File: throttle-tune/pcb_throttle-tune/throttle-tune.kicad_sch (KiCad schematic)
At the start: 49 parts, among them IC1 ATMEGA8A-P, J1 3speedSw-in, J10 9V supply / small battery, J2 gas-pedal-in, J3 throttle-out, J4 3speedSw-out, J5 UART [TX, RX, GND], J7 gpio-reserve, J8 reserve, reverse-sw, J9 5V/GND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

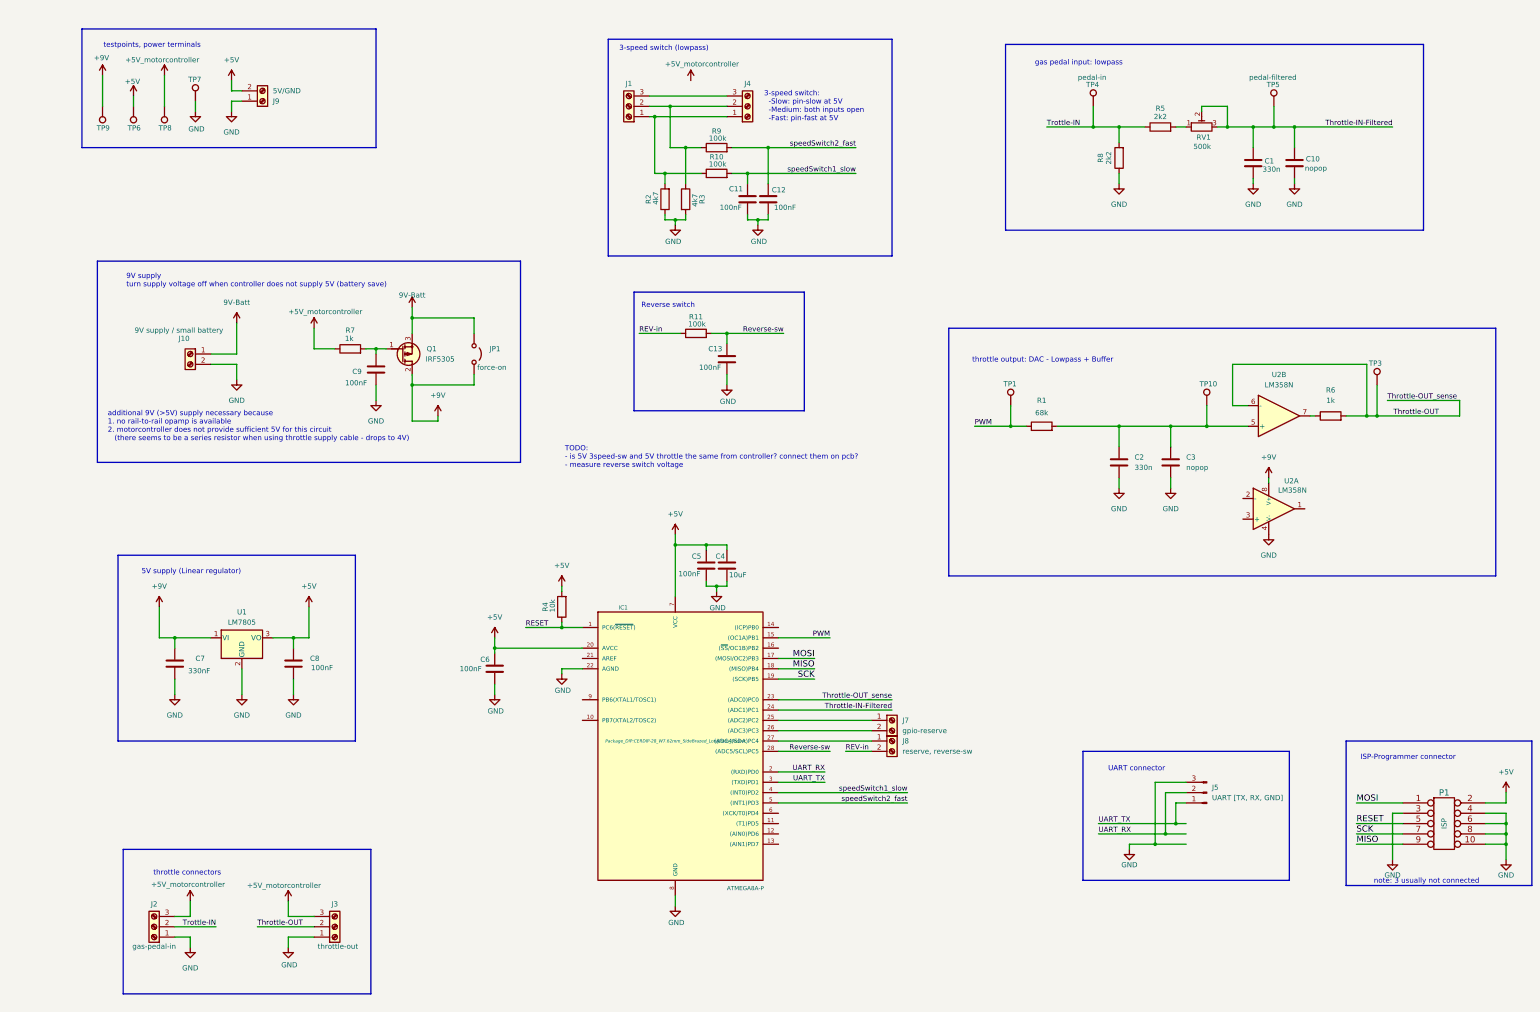
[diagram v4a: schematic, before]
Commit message: pcb: fix supply cutoff (add NPN), update layout
Note: fixed in already milled pcb by adding transistor with wires
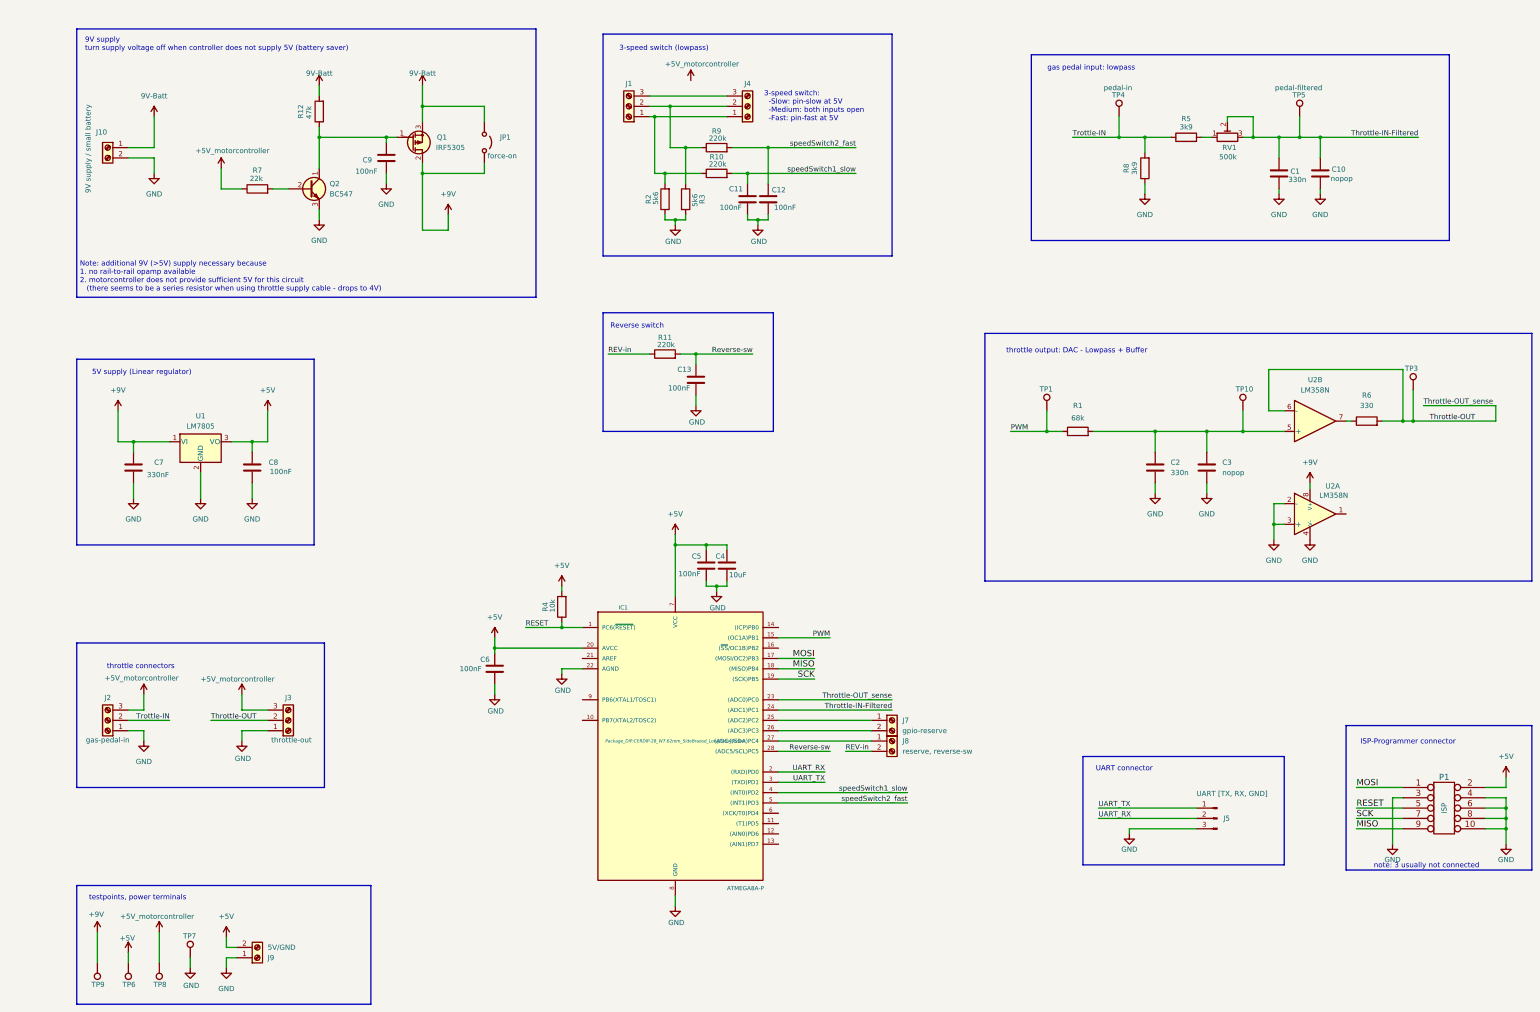
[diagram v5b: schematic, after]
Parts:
- added Q2: BC547, Package_TO_SOT_THT_AKL:TO-92_Inline_Wide_CBE, symbol Transistor_BJT_AKL:BC547
- added R12: 47k, Resistor_THT:R_Axial_DIN0207_L6.3mm_D2.5mm_P10.16mm_Horizontal, symbol Device:R
- R10, R11, R9: value 100k -> 220k
- R2, R3: value 4k7 -> 5k6
- R5, R8: value 2k2 -> 3k9
- R6: value 1k -> 330
- R7: value 1k -> 22k
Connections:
- net 9V-Batt: now also R12.2
- net GND: now also U2.2 (-), U2.3 (+), Q2.3 (E)
- net at C9.1, Q1.1 (G): now also Q2.1 (C), R12.1; no longer R7.2
- new net: Q2.2 (B), R7.2
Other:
- note added: "9V supply turn supply voltage off when controller does not supply 5V (battery saver)"
- note added: "Note: additional 9V (>5V) supply necessary because 1. no rail-to-rail opamp available 2. motorcontroller does not provide sufficient 5V for this circuit (there seems to be a series resistor when using throttle supply cable - drops to 4V)"
- note removed: "9V supply turn supply voltage off when controller does not supply 5V (battery save)"
- note removed: "TODO: - is 5V 3speed-sw and 5V throttle the same from controller? connect them on pcb? - measure reverse switch voltage"
- note removed: "additional 9V (>5V) supply necessary because 1. no rail-to-rail opamp is available 2. motorcontroller does not provide sufficient 5V for this circuit (there seems to be a series resistor when using throttle supply cable - drops to 4V)"
- moved on the sheet: C1, C10, C13, C2, C3, C7, C8, C9, J10, J2, J3, J5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

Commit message: pcb: optimize text, comments, Add README
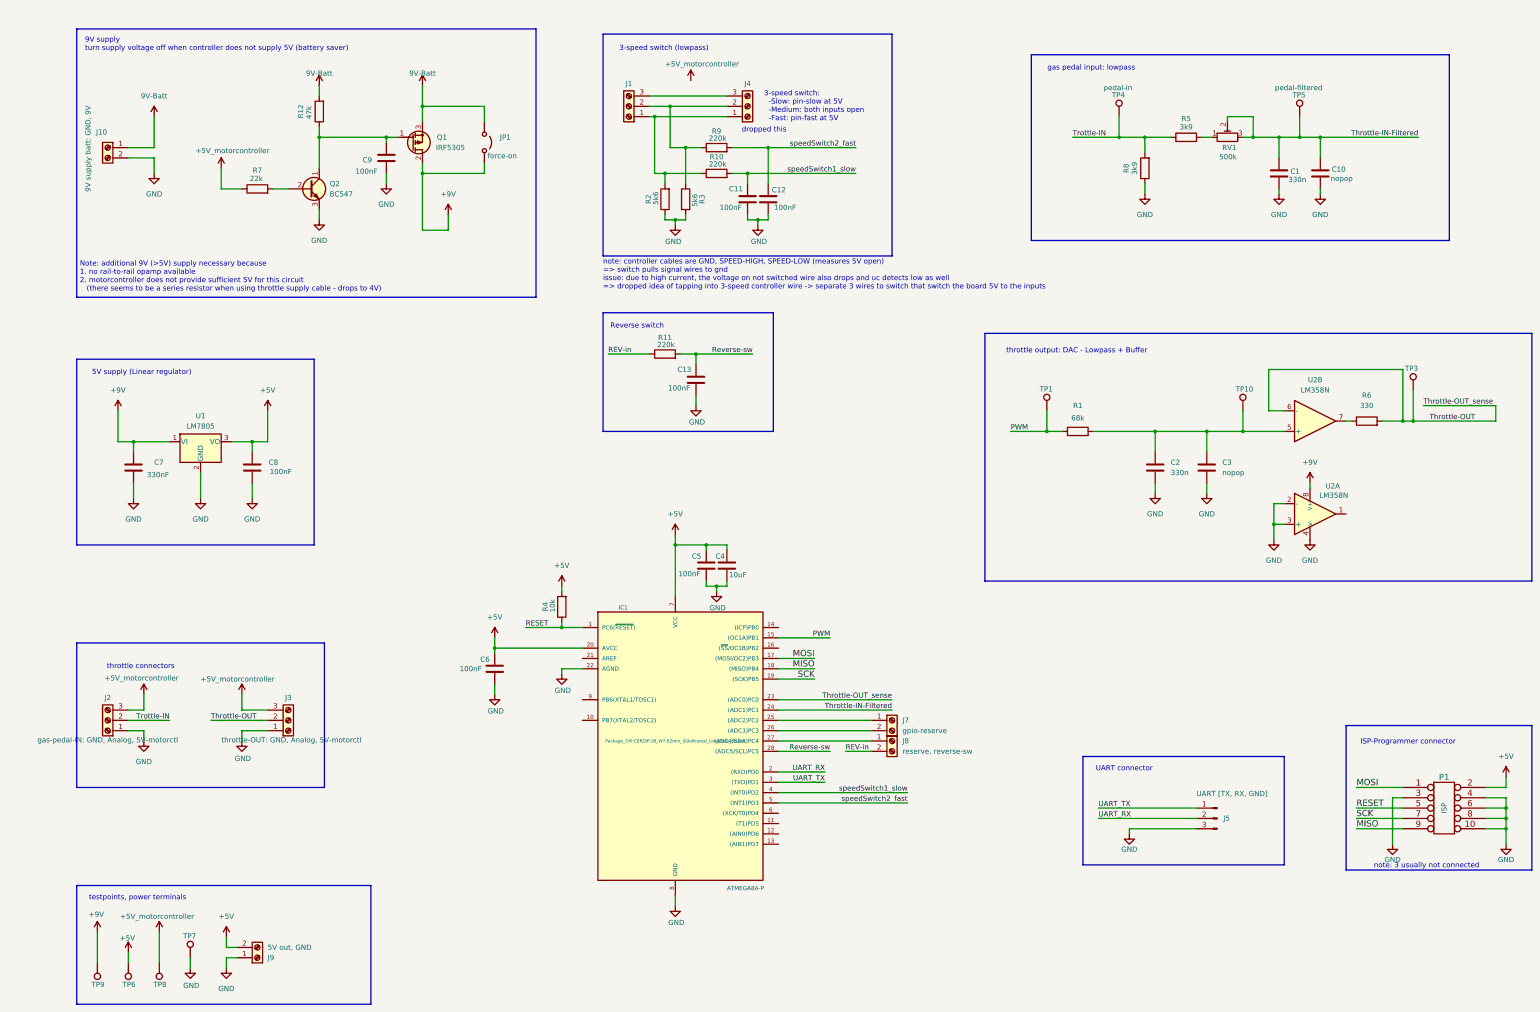
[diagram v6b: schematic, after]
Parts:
- J1: value 3speedSw-in -> 3-speed-IN: COM, sw-fast, sw-slow
- J10: value 9V supply / small battery -> 9V supply batt: GND, 9V
- J2: value gas-pedal-in -> gas-pedal-IN: GND, Analog, 5V-motorctl
- J3: value throttle-out -> throttle-OUT: GND, Analog, 5V-motorctl
- J4: value 3speedSw-out -> 3-speed-OUT: COM, sw-fast, sw-slow
- J9: value 5V/GND -> 5V out, GND
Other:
- note added: "dropped this"
- note added: "note: controller cables are GND, SPEED-HIGH, SPEED-LOW (measures 5V open) => switch pulls signal wires to gnd issue: due to high current, the voltage on not switched wire also drops and uc detects low as well => dropped idea of tapping into 3-speed controller wire -> separate 3 wires to switch that switch the board 5V to the inputs"
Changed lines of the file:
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@@
 		)
 	)
+	(text "note: controller cables are GND, SPEED-HIGH, SPEED-LOW (measures 5V open)\n=> switch pulls signal wires to gnd\nissue: due to high current, the voltage on not switched wire also drops and uc detects low as well\n=> dropped idea of tapping into 3-speed controller wire -> separate 3 wires to switch that switch the board 5V to the inputs"
+		(exclude_from_sim no)
+		(at 151.13 82.042 0)
+		(effects
+			(font
+				(size 1.27 1.27)
+			)
+			(justify left)
+		)
+	)
 	(text "throttle connectors\n"
 		(exclude_from_sim no)
@@
 		)
 	)
+	(text "dropped this"
+		(exclude_from_sim no)
+		(at 190.754 46.482 0)
+		(effects
+			(font
+				(size 1.27 1.27)
+			)
+		)
+	)
 	(text "gas pedal input: lowpass"
 		(exclude_from_sim no)
@@
 			)
 		)
-		(property "Value" "5V/GND"
+		(property "Value" "5V out, GND"
 			(at 68.58 247.6501 0)
 			(effects
@@
 			)
 		)
-		(property "Value" "throttle-out"
+		(property "Value" "throttle-OUT: GND, Analog, 5V-motorctl"
 			(at 74.422 196.596 0)
 			(effects
@@
 			)
 		)
-		(property "Value" "3speedSw-in"
+		(property "Value" "3-speed-IN: COM, sw-fast, sw-slow"
 			(at 156.464 34.798 0)
 			(effects
@@
 			)
 		)
-		(property "Value" "9V supply / small battery"
+		(property "Value" "9V supply batt: GND, 9V"
 			(at 24.384 51.054 90)
 			(effects
@@
 			)
 		)
-		(property "Value" "3speedSw-out"
+		(property "Value" "3-speed-OUT: COM, sw-fast, sw-slow"
 			(at 187.706 34.798 0)
 			(effects
@@
 			)
 		)
-		(property "Value" "gas-pedal-in"
+		(property "Value" "gas-pedal-IN: GND, Analog, 5V-motorctl"
 			(at 29.21 196.596 0)
 			(effects
